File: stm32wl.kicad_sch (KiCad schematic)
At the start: 25 parts, among them U201 STM32WLE5CCUx

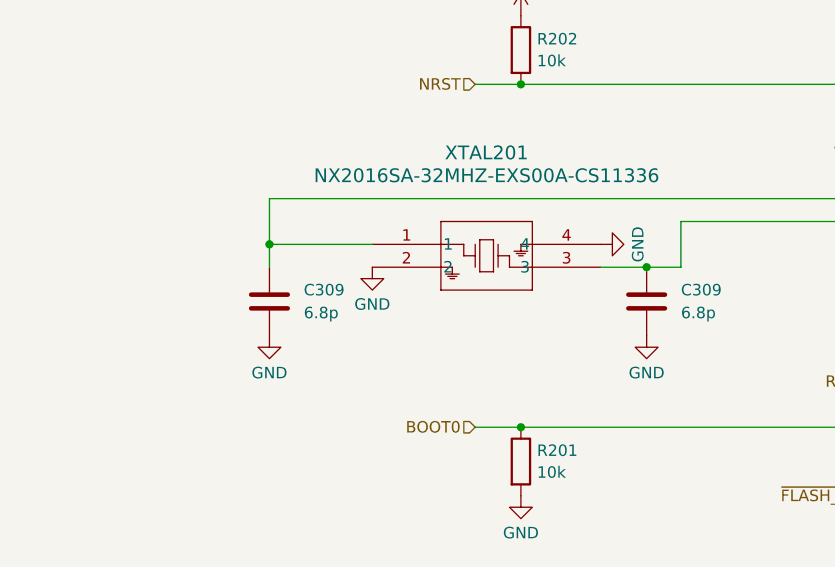
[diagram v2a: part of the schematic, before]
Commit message: bom tweaks
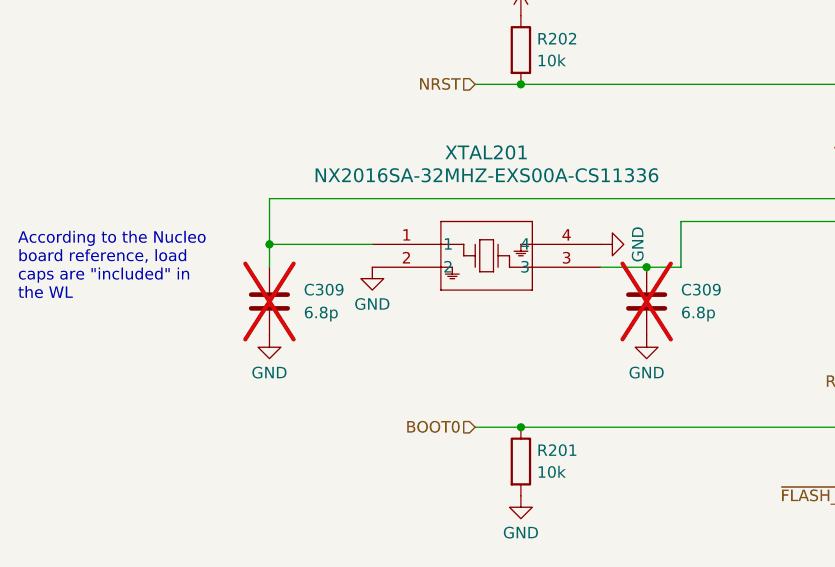
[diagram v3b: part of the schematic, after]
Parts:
- C309: now not fitted
- L202: Part (none) -> MLZ2012M150W
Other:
- note added: "According to the Nucleo board reference, load caps are "included" in the WL"
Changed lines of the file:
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@@
     (stroke (width 0) (type default))
+  )
+  (text "According to the Nucleo\nboard reference, load\ncaps are \"included\" in \nthe WL"
+    (at 21.59 80.01 0)
+    (effects (font (size 1.27 1.27)) (justify left bottom))
   )
   (label "VDDRF1V55" (at 157.48 48.26 90) (fields_autoplaced)
@@
   )
   (symbol (lib_id "Device:C") (at 91.44 80.01 0) (unit 1)
-    (in_bom yes) (on_board yes) (dnp no) (fields_autoplaced)
+    (in_bom yes) (on_board yes) (dnp yes) (fields_autoplaced)
     (property "Reference" "C309" (at 95.25 78.74 0)
       (effects (font (size 1.27 1.27)) (justify left))
@@
       (effects (font (size 1.27 1.27)) hide)
     )
+    (property "Part" "MLZ2012M150W" (at 97.79 181.61 90)
+      (effects (font (size 1.27 1.27)) hide)
+    )
     (pin "1")
     (pin "2")
@@
   )
   (symbol (lib_id "Device:C") (at 49.53 80.01 180) (unit 1)
-    (in_bom yes) (on_board yes) (dnp no) (fields_autoplaced)
+    (in_bom yes) (on_board yes) (dnp yes) (fields_autoplaced)
     (property "Reference" "C309" (at 53.34 78.74 0)
       (effects (font (size 1.27 1.27)) (justify right))

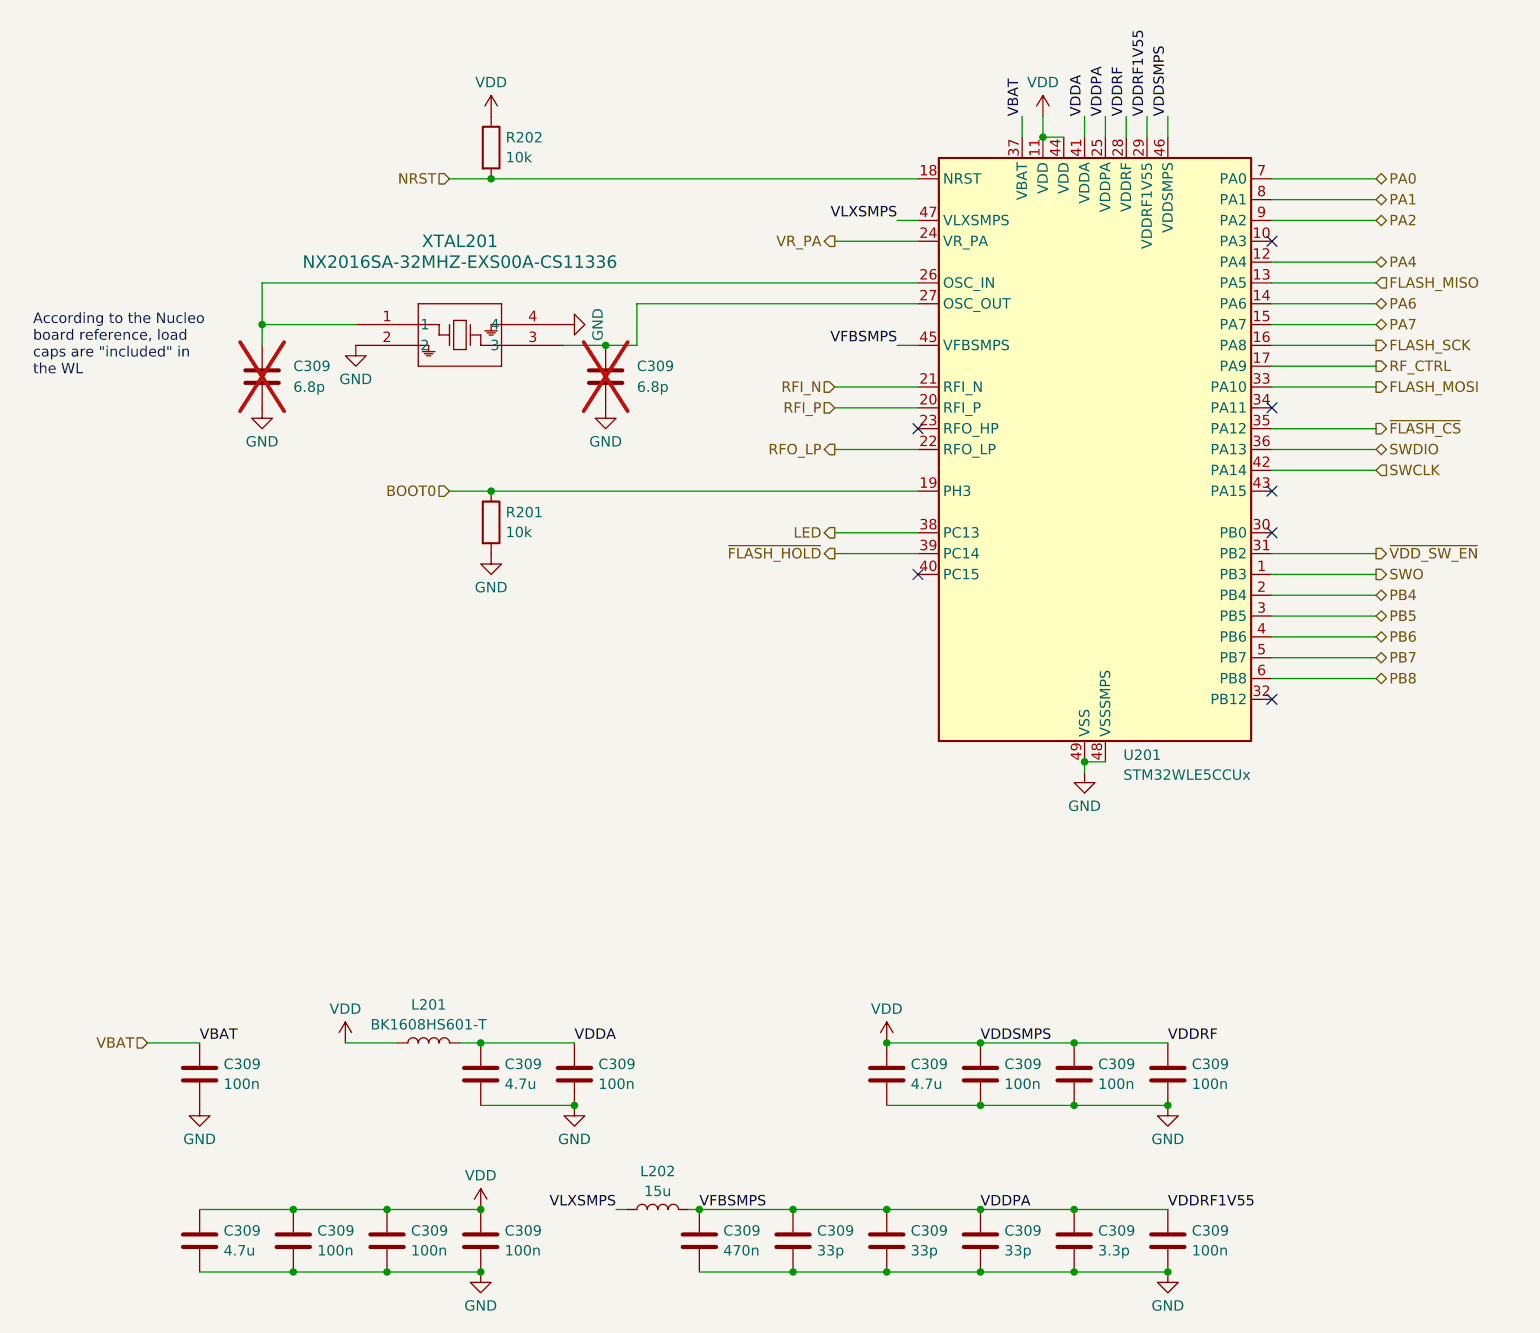
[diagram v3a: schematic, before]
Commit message: changed XO to TCXO
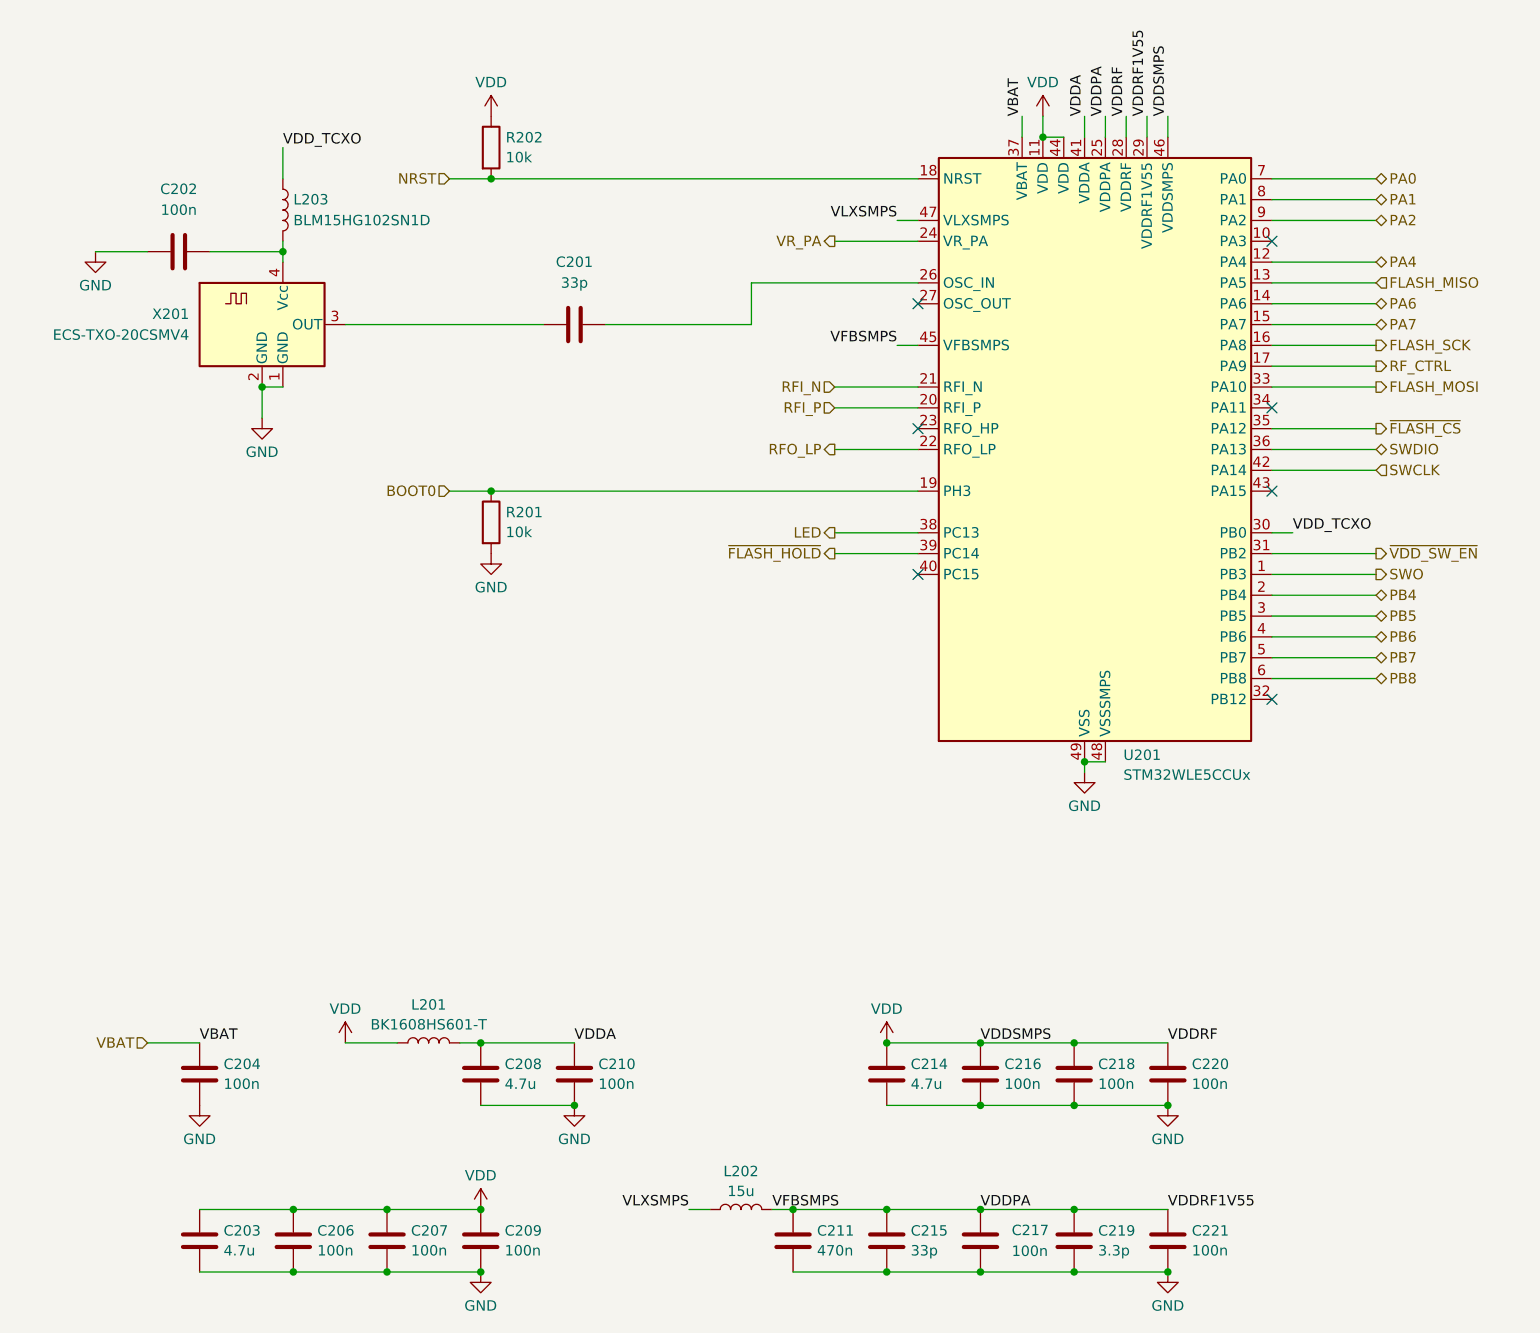
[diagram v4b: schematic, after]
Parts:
- removed C309 (x2): 6.8p, Capacitor_SMD:C_0402_1005Metric, symbol Device:C
- removed C309: 33p, Capacitor_SMD:C_0402_1005Metric, symbol Device:C
- removed XTAL201: NX2016SA-32MHZ-EXS00A-CS11336, lora-module:NX2016SA_NDK, symbol NX2016SA_NDK-CS11336-32M:NX2016SA-32MHZ-EXS00A-CS11336
- added C201: 33p, Capacitor_SMD:C_0402_1005Metric, symbol Device:C
- added C202: 100n, Capacitor_SMD:C_0402_1005Metric, symbol Device:C
- added L203: BLM15HG102SN1D, Inductor_SMD:L_0402_1005Metric, symbol Device:L
- added X201: ECS-TXO-20CSMV4, lora-module:NX2016SA_NDK, symbol ECS-TXO-20CSMV4:ECS-TXO-20CSMV4
- C217: renamed from C309; value 33p -> 100n
- renumbered C309 to C203, C309 to C204, C309 to C206, C309 to C207, C309 to C208, C309 to C209, C309 to C210, C309 to C211, C309 to C214, C309 to C215, C309 to C216, C309 to C218, C309 to C219, C309 to C220, C309 to C221
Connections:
- net GND: now also C202.1, X201.1 (GND), X201.2 (GND)
- net at U201.26 (OSC_IN): now also C201.2
- net VDD_TCXO: now reaches U201.30 (PB0)
- net VDD_TCXO: now also L203.1
- new net: C201.1, X201.3 (OUT)
- new net: C202.2, L203.2, X201.4 (Vcc)
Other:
- note removed: "According to the Nucleo board reference, load caps are "included" in the WL"
- moved on the sheet: C211, L202

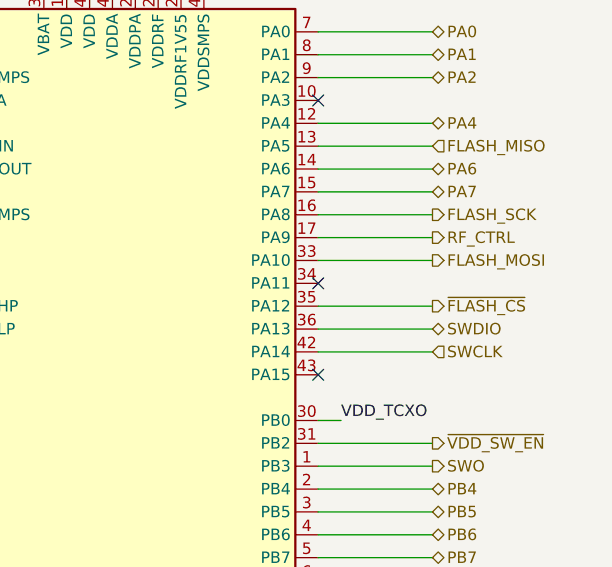
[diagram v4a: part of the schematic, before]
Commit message: module pinout change
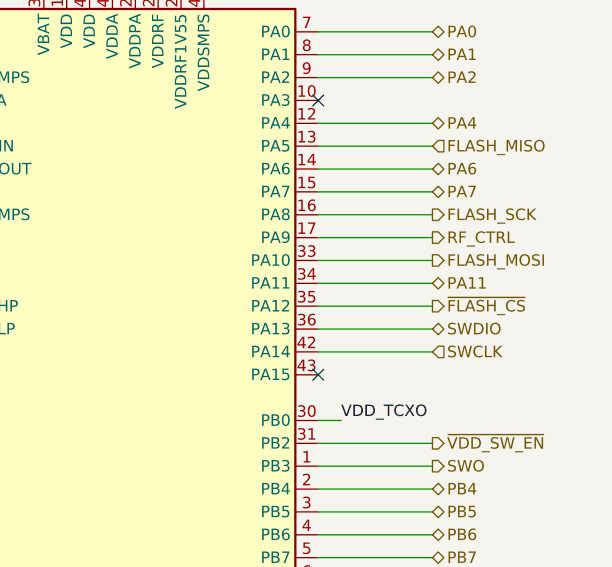
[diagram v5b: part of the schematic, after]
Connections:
- net PA11: now reaches U201.34 (PA11)
- no-connect marks 7 -> 6
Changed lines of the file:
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@@
   (junction (at 148.59 189.23) (diameter 0) (color 0 0 0 0)
   )
-  (no_connect (at 172.72 83.82))
   (no_connect (at 129.54 104.14))
   (no_connect (at 172.72 63.5))
@@
     (stroke (width 0) (type default))
   )
+  (wire (pts (xy 172.72 83.82) (xy 185.42 83.82))
+    (stroke (width 0) (type default))
+  )
   (wire (pts (xy 52.07 52.07) (xy 52.07 55.88))
     (stroke (width 0) (type default))
@@
     (effects (font (size 1.27 1.27)) (justify right))
   )
+  (hierarchical_label "PA11" (shape bidirectional) (at 185.42 83.82 0) (fields_autoplaced)
+    (effects (font (size 1.27 1.27)) (justify left))
+  )
   (hierarchical_label "PB7" (shape bidirectional) (at 185.42 114.3 0) (fields_autoplaced)

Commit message: bom update and other tweaks
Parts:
- removed C201: 33p, Capacitor_SMD:C_0402_1005Metric, symbol Device:C
- added C1: 39p, Capacitor_SMD:C_0402_1005Metric, symbol Device:C
- L202: value 15u -> 15uH; Part MLZ2012M150W -> MLZ2012M150WT000
- U201: value STM32WLE5CCUx -> STM32WLE5CCU6
- X201: value ECS-TXO-20CSMV4 -> ECS-TXO-20CSMV4-320-AY-TR
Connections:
- net at U201.26 (OSC_IN): now also C1.2
- net at X201.3 (OUT): now also C1.1
